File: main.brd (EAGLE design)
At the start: 160 x 100 mm, 22 parts, among them U1 ATSAMD21G-A

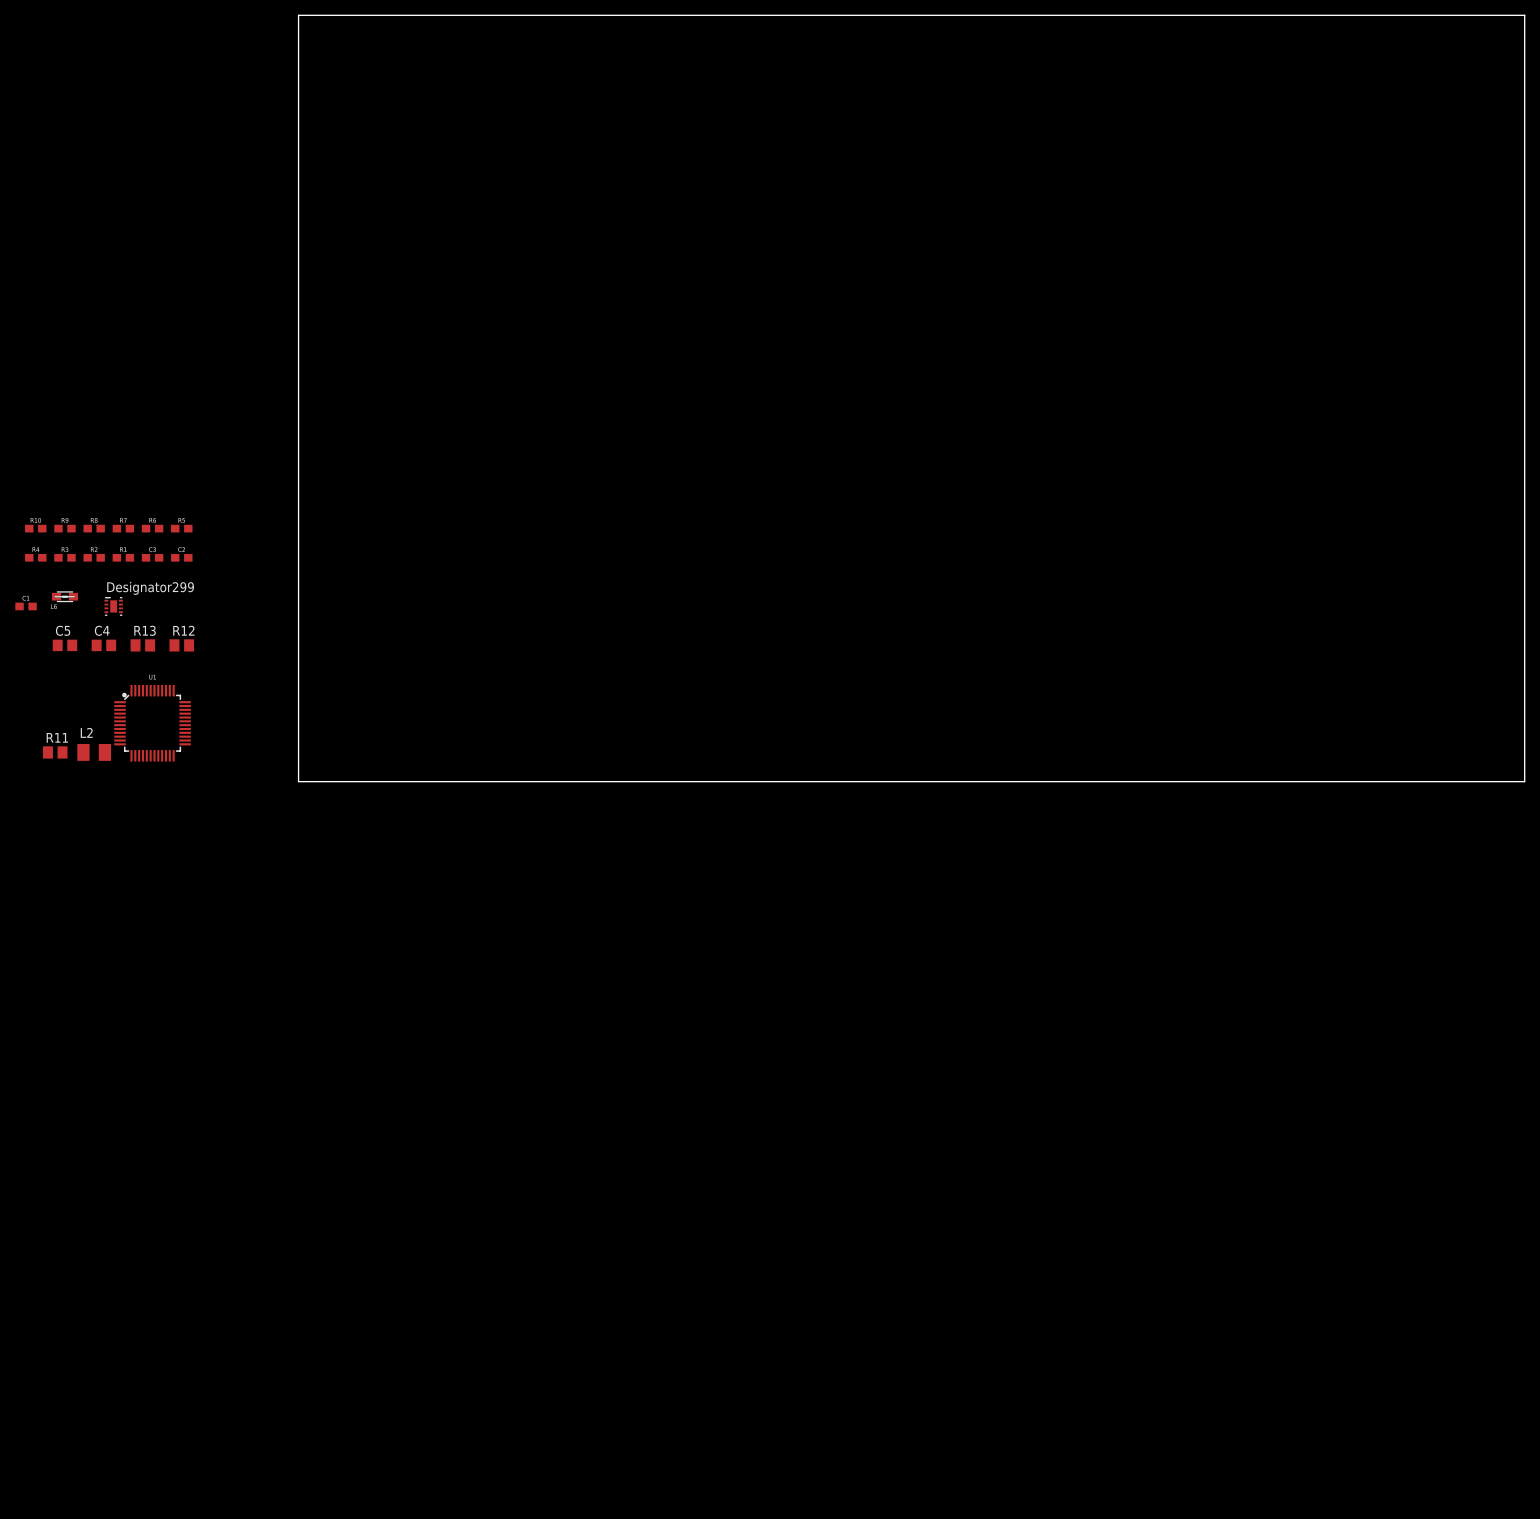
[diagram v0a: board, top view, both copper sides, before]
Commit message: Added SD, AIO, and Valve State IO
Added Analog IO ports along with modified voltage dividers.

Added valve state ports, and a connected state jumper.

Added SD card, and conencted it SPI bus, unsure what CD pins are, and if RSV pings need to be connected at all.
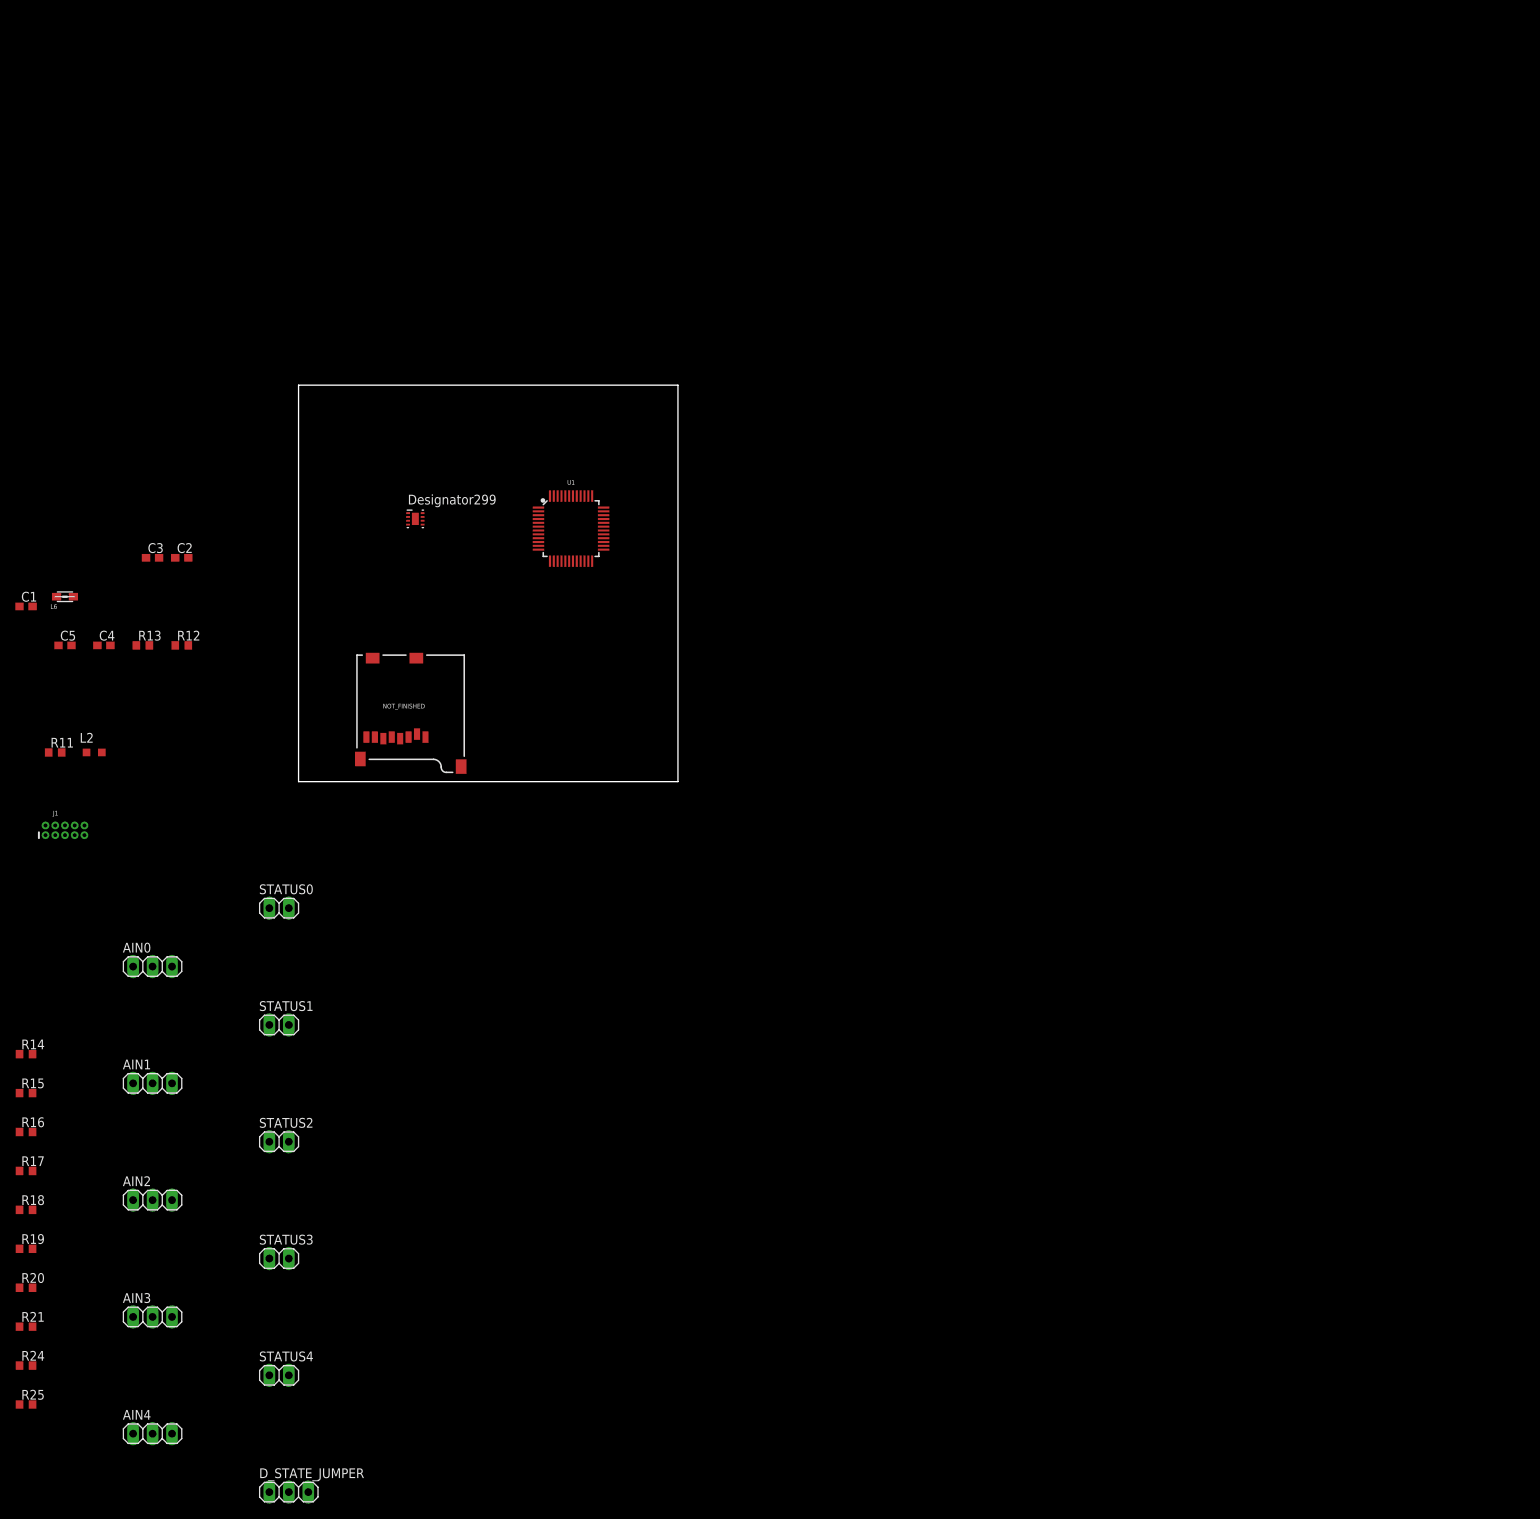
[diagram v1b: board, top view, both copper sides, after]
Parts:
- removed R1, R10, R2, R3, R4, R5, R6, R7, R8, R9: 1k, SparkFun-Resistors:0603
- added AIN0, AIN1, AIN2, AIN3, AIN4, D_STATE_JUMPER: (no value), pinhead:1X03
- added J1: CORTEX_DEBUG_PTH, SparkFun-Connectors:2X5-PTH-1.27MM
- added NOT_FINISHED: MICRO-SD_CARD_SOCKET, SparkFun-Connectors:MICRO-SD-SOCKET
- added R14, R15, R16, R17, R18: 1.32k, resistor:R0603
- added R19, R20, R21, R24, R25: 680, resistor:R0603
- added STATUS0, STATUS1, STATUS2, STATUS3, STATUS4: (no value), pinhead:1X02
- C1, C2, C3: device SparkFun-Capacitors:0603 -> resistor:C0603
- C4, C5: device resistor:C0805 -> resistor:C0603
- L2: device resistor:L3225M -> resistor:L2012C
- R11, R12, R13: device resistor:M0805 -> resistor:R0603
- moved U1 60.2 mm to (35.6, 33.0)
- moved PWR_REG 41.0 mm to (15.2, 34.3)
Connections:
- net PG_REG renamed PG
- removed net 5V_AIN0: R9.2
- removed net 5V_AIN2: R3.2
- removed net 5V_AIN3: R1.2
- removed net 5V_AIN4: R7.2
- removed net 5V_AIN5: R5.2
- removed net PB08_AIN1: R5.1, R6.1
- new net D_STATE: D_STATE_JUMPER.2, STATUS0.1, STATUS1.1, STATUS2.1, STATUS3.1, STATUS4.1
- new net GPIO_IN_0: STATUS0.2
- new net GPIO_IN_1: STATUS1.2
- new net GPIO_IN_2: STATUS2.2
- new net GPIO_IN_3: STATUS3.2
- new net GPIO_IN_4: STATUS4.2
- new net N$1: AIN1.3, R20.1
- new net N$3: AIN2.3, R21.1
- new net N$4: AIN3.3, R24.1
- new net N$5: AIN4.3, R25.1
- new net N$8: AIN0.3, R19.1
- new net PA30_SWCLK: J1.4, U1.45
- new net PA31_SWDIO: J1.2, U1.46
- new net ~RESET: J1.10, U1.40
- new net ~SD_CS: NOT_FINISHED.CS
- net 3.3V: now also D_STATE_JUMPER.1, J1.1, NOT_FINISHED.VCC
- net GND: now also AIN0.2, AIN1.2, AIN2.2, AIN3.2, AIN4.2, D_STATE_JUMPER.3, J1.3, J1.5, J1.9, NOT_FINISHED.GND, NOT_FINISHED.GND1, NOT_FINISHED.GND3, R14.2, R15.2, R16.2, R17.2, R18.2; no longer R10.2, R2.2, R4.2, R6.2, R8.2
- net PA02_AIN0: now also R14.1, R19.2; no longer R10.1, R9.1
- net PA04_AIN4: now also R15.1, R20.2; no longer R7.1, R8.1
- net PA05_AIN5: now also R16.1, R21.2
- net PB08_AIN2: now also R17.1, R24.2; no longer R3.1, R4.1
- net PB09_AIN3: now also R18.1, R25.2; no longer R1.1, R2.1
- net SPI_MISO: now also NOT_FINISHED.DO
- net SPI_MOSI: now also NOT_FINISHED.DI
- net SPI_SCK: now also NOT_FINISHED.SCLK
- net VIN: now also AIN0.1, AIN1.1, AIN2.1, AIN3.1, AIN4.1
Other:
- board size 160 x 100 mm -> 49.5 x 51.7 mm

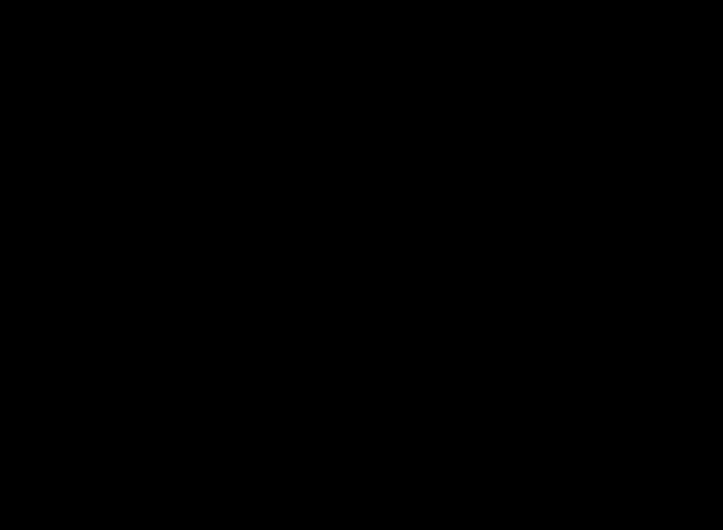
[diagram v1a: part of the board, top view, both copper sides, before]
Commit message: Added IMU and Battery Controller
Battery Controller IC may be wrong
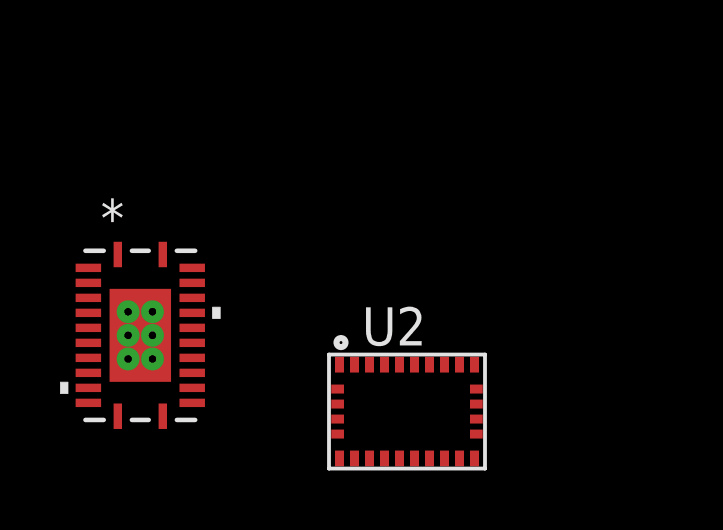
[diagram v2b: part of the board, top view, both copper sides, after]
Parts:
- added U2: BNO055, BNO055:LGA28R50P4X10_380X520X100
- added U3: BQ24133_RGY_24, BQ24133:RGY24_2P05X3P1
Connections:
- new net AVCC: U3.4
- new net BTST: U3.21
- new net EPAD: U3.25
- new net GNDIO: U2.25
- new net PGND: U3.23
- new net PGND_2: U3.22
- new net PIN10: U2.10
- new net PIN15: U2.15
- new net PIN16: U2.16
- new net PVCC: U3.3
- new net PVCC_2: U3.2
- new net REGN: U3.20
- new net SW: U3.24
- new net SW_2: U3.1
- new net VDD: U2.3
- new net VDDIO: U2.28
- new net VREF: U3.12
- net GND: now also U2.2
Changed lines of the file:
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@@
 <attribute name="SF_ID" value="PRT-00127" x="7.62" y="16.51" size="1.778" layer="27" rot="R180" display="off"/>
+</element>
+<element name="U2" library="BNO055" package="LGA28R50P4X10_380X520X100" value="BNO055" x="-34.29" y="-105.41">
+<attribute name="AVAILABILITY" value="Good" x="-34.29" y="-105.41" size="1.778" layer="27" display="off"/>
+<attribute name="DESCRIPTION" value="IMU ACCEL/GYRO/MAG I2C 28LGA" x="-34.29" y="-105.41" size="1.778" layer="27" display="off"/>
+<attribute name="MF" value="Bosch" x="-34.29" y="-105.41" size="1.778" layer="27" display="off"/>
+<attribute name="MP" value="BNO055" x="-34.29" y="-105.41" size="1.778" layer="27" display="off"/>
+<attribute name="PACKAGE" value="LGA-28 Bosch" x="-34.29" y="-105.41" size="1.778" layer="27" display="off"/>
+<attribute name="PRICE" value="7.78 USD" x="-34.29" y="-105.41" size="1.778" layer="27" display="off"/>
+</element>
+<element name="U3" library="BQ24133" package="RGY24_2P05X3P1" value="BQ24133_RGY_24" x="-43.18" y="-102.87">
+<attribute name="DATASHEETURL" value="httpwww.ti.comlitgpnBQ24133" x="-43.18" y="-102.87" size="1.778" layer="27" display="off"/>
+<attribute name="FAMILY_NAME" value="BATTERY CHARGE MANAGEMENT" x="-43.18" y="-102.87" size="1.778" layer="27" display="off"/>
+<attribute name="GENERIC_PART_NUMBER" value="BQ24133" x="-43.18" y="-102.87" size="1.778" layer="27" display="off"/>
+<attribute name="INDUSTRY_STD_PKG_TYPE" value="VQFN" x="-43.18" y="-102.87" size="1.778" layer="27" display="off"/>
+<attribute name="MANUFACTURER" value="Texas Instruments" x="-43.18" y="-102.87" size="1.778" layer="27" display="off"/>
+<attribute name="PACKAGE_DESIGNATOR" value="RGY" x="-43.18" y="-102.87" size="1.778" layer="27" display="off"/>
+<attribute name="PIN_COUNT" value="24" x="-43.18" y="-102.87" size="1.778" layer="27" display="off"/>
 </element>
 </elements>
@@
 <contactref element="NOT_FINISHED" pad="GND3"/>
 <contactref element="NOT_FINISHED" pad="GND1"/>
+<contactref element="U2" pad="2"/>
+<wire x1="-19.05" y1="-85.09" x2="-36.6025" y2="-104.66" width="0" layer="19" extent="1-1"/>
 <wire x1="-19.05" y1="-69.85" x2="-19.05" y2="-85.09" width="0" layer="19" extent="1-1"/>
 <wire x1="-19.05" y1="-54.61" x2="-19.05" y2="-69.85" width="0" layer="19" extent="1-1"/>
@@
 <wire x1="15.24" y1="34.290003125" x2="14.29" y2="33.54" width="0" layer="19" extent="1-1"/>
 <wire x1="14.29" y1="35.04" x2="15.24" y2="34.290003125" width="0" layer="19" extent="1-1"/>
-<wire x1="31.31" y1="33.77" x2="14.29" y2="33.54" width="0" layer="19" extent="1-1"/>
+<wire x1="31.31" y1="33.77" x2="15.24" y2="34.290003125" width="0" layer="19" extent="1-1"/>
 <wire x1="35.81" y1="37.27" x2="31.31" y2="33.77" width="0" layer="19" extent="1-1"/>
 <wire x1="39.81" y1="35.27" x2="35.81" y2="37.27" width="0" layer="19" extent="1-1"/>
 <wire x1="35.31" y1="28.77" x2="31.31" y2="33.77" width="0" layer="19" extent="1-1"/>
-<wire x1="8.07" y1="2.96" x2="1.27" y2="-92.71" width="0" layer="19" extent="1-1"/>
-<wire x1="11.06" y1="5.61" x2="8.07" y2="2.96" width="0" layer="19" extent="1-1"/>
+<wire x1="11.06" y1="5.61" x2="14.29" y2="33.54" width="0" layer="19" extent="1-1"/>
+<wire x1="8.07" y1="2.96" x2="11.06" y2="5.61" width="0" layer="19" extent="1-1"/>
 <wire x1="21.22" y1="1.96" x2="11.06" y2="5.61" width="0" layer="19" extent="1-1"/>
 </signal>
@@
 <contactref element="NOT_FINISHED" pad="CS"/>
 </signal>
+<signal name="VDD">
+<contactref element="U2" pad="3"/>
+</signal>
+<signal name="PIN10">
+<contactref element="U2" pad="10"/>
+</signal>
+<signal name="PIN15">
+<contactref element="U2" pad="15"/>
+</signal>
+<signal name="PIN16">
+<contactref element="U2" pad="16"/>
+</signal>
+<signal name="GNDIO">
+<contactref element="U2" pad="25"/>
+</signal>
+<signal name="VDDIO">
+<contactref element="U2" pad="28"/>
+</signal>
+<signal name="SW_2">
+<contactref element="U3" pad="1"/>
+</signal>
+<signal name="PVCC_2">
+<contactref element="U3" pad="2"/>
+</signal>
+<signal name="PVCC">
+<contactref element="U3" pad="3"/>
+</signal>
+<signal name="AVCC">
+<contactref element="U3" pad="4"/>
+</signal>
+<signal name="VREF">
+<contactref element="U3" pad="12"/>
+</signal>
+<signal name="REGN">
+<contactref element="U3" pad="20"/>
+</signal>
+<signal name="BTST">
+<contactref element="U3" pad="21"/>
+</signal>
+<signal name="PGND_2">
+<contactref element="U3" pad="22"/>
+</signal>
+<signal name="PGND">
+<contactref element="U3" pad="23"/>
+</signal>
+<signal name="SW">
+<contactref element="U3" pad="24"/>
+</signal>
+<signal name="EPAD">
+<contactref element="U3" pad="25"/>
+</signal>
 </signals>
